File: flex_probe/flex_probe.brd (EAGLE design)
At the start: 94 x 12 mm, 7 parts

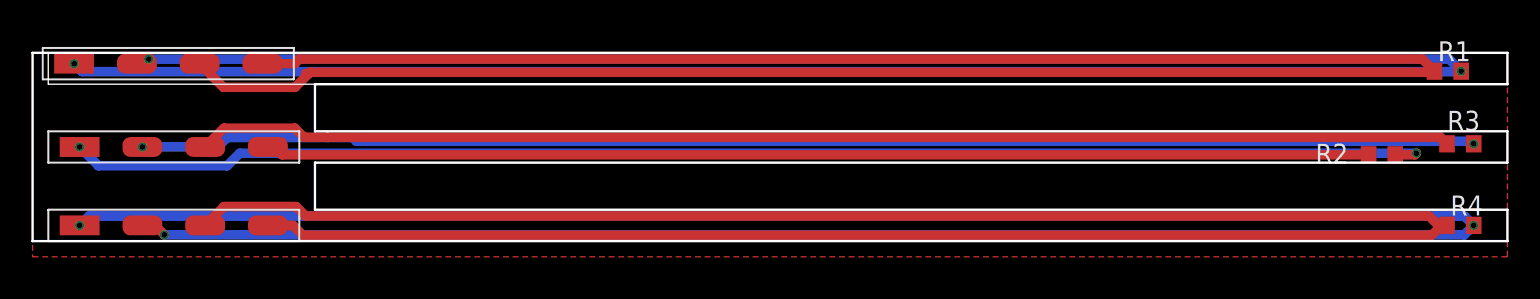
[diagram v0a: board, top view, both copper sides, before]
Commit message: New flex PCB.
Shorter length to decrease cost.
Larger trace widths to reduce resistance.
Through-hole connections to make wiring easier
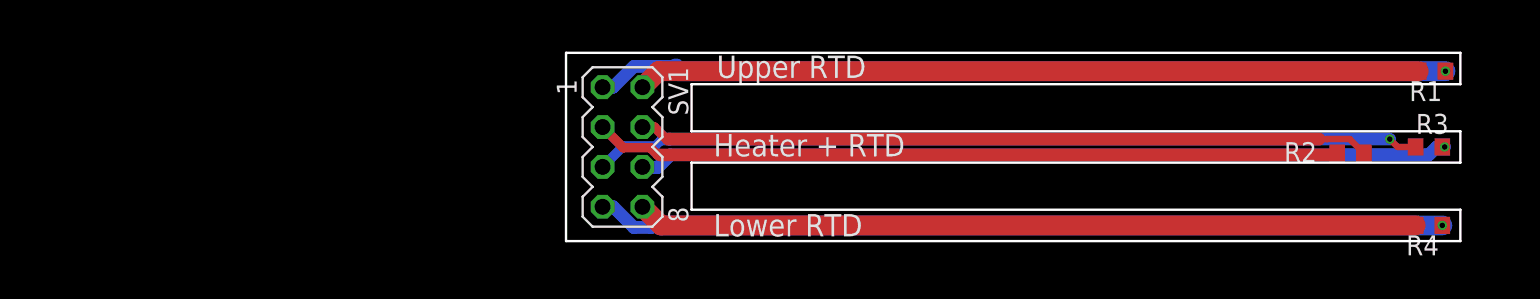
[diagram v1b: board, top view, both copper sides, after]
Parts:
- removed U$1, U$2, U$3: CONN_1X4, marshal:4PAD
- added SV1: (no value), con-lstb:MA04-2
- R1, R2, R4: value (none) -> RTD
- R3: value (none) -> 50
- moved R3 2.01 mm to (115.0, 32.0)
- moved R2 2.00 mm to (110.0, 31.6)
- moved R4 2.00 mm to (115.0, 27.0), turned to 180 degrees
- moved R1 1.00 mm to (115.2, 36.8), turned to 180 degrees
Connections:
- removed net N$10: R4.2, U$3.P$1, U$3.P$2
- removed net N$6: R2.1, U$2.P$4
- new net N$3: R2.2, SV1.4
- new net N$4: R2.1, SV1.3
- net N$1: now also SV1.2; no longer U$1.P$1, U$1.P$2
- net N$11: now also R4.2, SV1.8; no longer R4.1, U$3.P$3, U$3.P$4
- net N$2: now also SV1.1; no longer U$1.P$3, U$1.P$4
- net N$7: now also R4.1, SV1.7; no longer R3.2, U$2.P$2
- net N$8: now also R3.2, SV1.6; no longer R3.1, U$2.P$3
- net N$9: now also R3.1, SV1.5; no longer R2.2, U$2.P$1
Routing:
- net N$10: track 174.7 -> 0.00 mm, vias 3 -> 0
- net N$1: track 173.5 -> 49.9 mm, vias 3 -> 0
- net N$11: track 155.8 -> 49.8 mm
- net N$2: track 155.1 -> 54.4 mm, vias 0 -> 1
- net N$6: track 70.4 -> 0.00 mm
- net N$4: track 0.00 -> 47.6 mm
- net N$3: track 0.00 -> 46.7 mm
- net N$9: track 87.4 -> 53.2 mm, vias 2 -> 1
- net N$7: track 85.8 -> 54.1 mm, vias 2 -> 1
- net N$8: track 80.1 -> 51.8 mm, vias 0 -> 1
- removed copper zone on layer 1, net N$5
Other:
- board size 94 x 12 mm -> 57 x 12 mm
- board text added: "1"
- board text added: "2"
- board text added: "3"
- board text added: "4"
- board text added: "Heater + RTD"
- board text added: "Lower RTD"
- board text added: "Upper RTD"
- board text removed: "Botm RTD"
- board text removed: "Heat+RTD"
- board text removed: "Top RTD"
